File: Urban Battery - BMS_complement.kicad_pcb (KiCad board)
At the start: 2 copper layers, 154 x 84.1 mm, 57 parts, among them J1 BMS IO, J10 E-Stop, J11 Contactor Connector, J12 Thermistor, J13 Thermistor, J14 Thermistor, J15 short pins, J16 short pins, J17 short pins, J18 short pins, J19 Test-pins, J2 OLED Header, J20 Test-pins, J21 Test-pins, J22 Test-pins, J23 Test-pins, J24 Test-pins, J25 Test-pins, J26 Test-pins, J27 Test-pins, J3 CAN, J4 CAN, J5 Charge Connector, J6 Battery Connector, J7 E-Stop, J8 E-Stop, J9 E-Stop, K1 Charge_Relay, K2 Contactor_Relay, SW1 SW_SPST, SW2 SW_DPDT_x2, SW3 CAN_TERM, U1 MCP2515-I/SO, U2 MCP2561/2, U3 LM2576HVS-12, Y1 8MHz

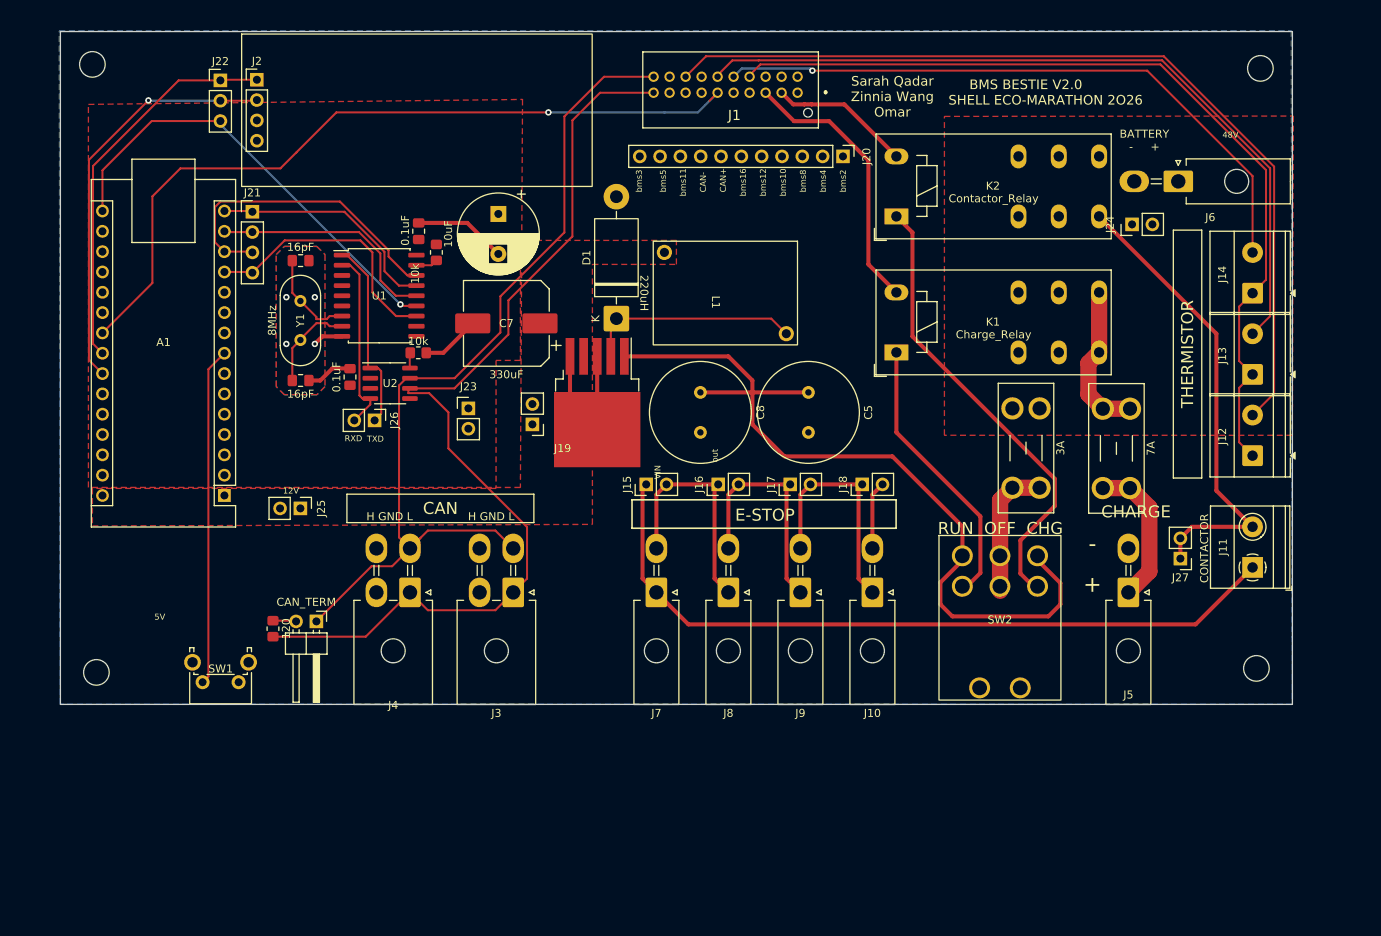
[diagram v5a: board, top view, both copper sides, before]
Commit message: routed BMS test pins, edited some labels
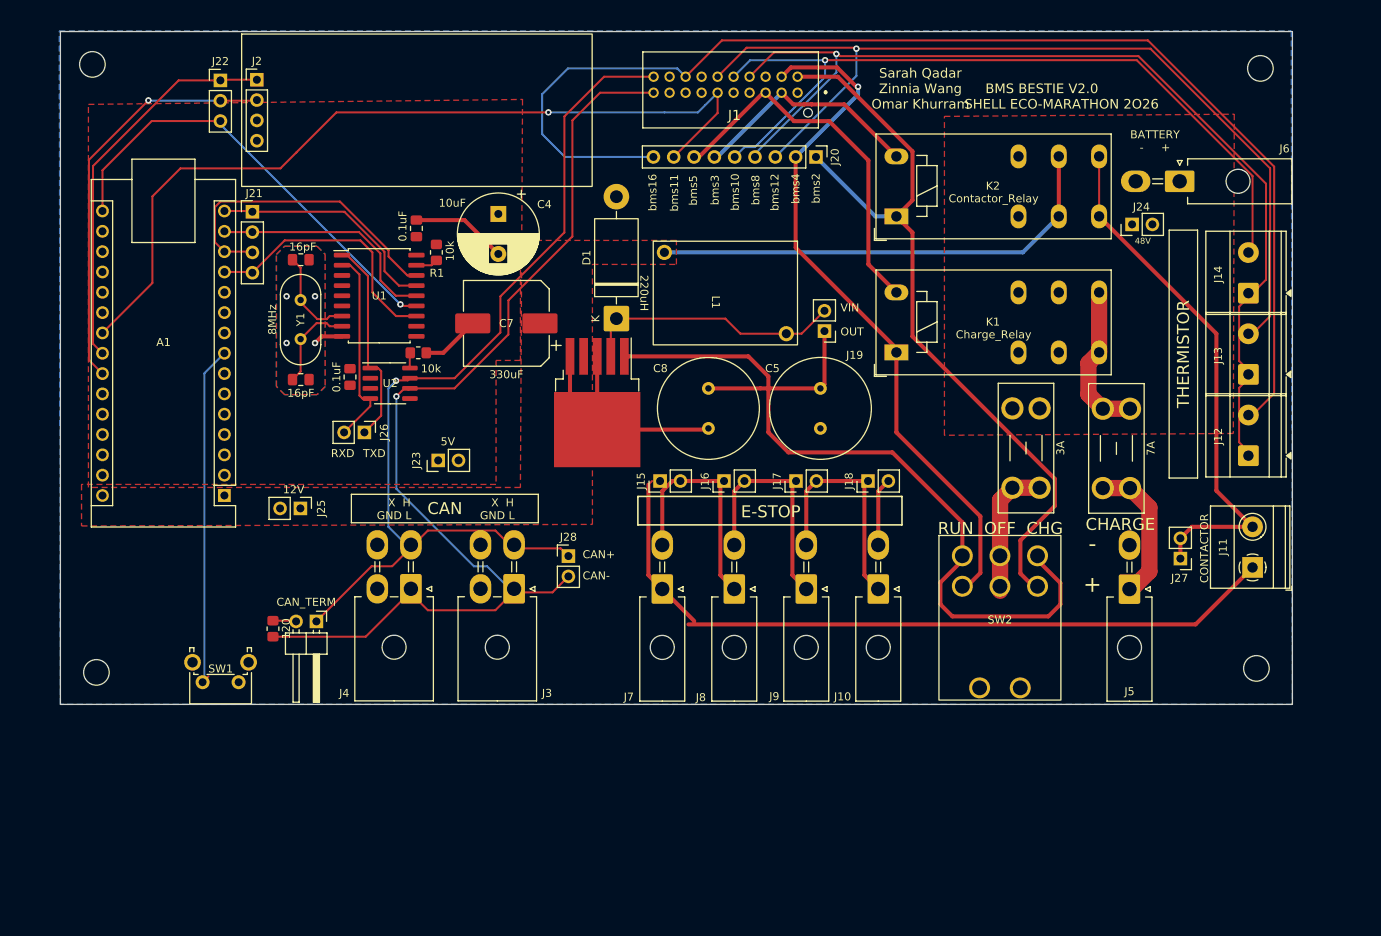
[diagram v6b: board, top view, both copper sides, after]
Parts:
- added J28: Test-pins, Connector_PinHeader_2.54mm:PinHeader_1x02_P2.54mm_Vertical, F.Cu at (138.0, 118.0)
- J20: footprint Connector_PinHeader_2.54mm:PinHeader_1x11_P2.54mm_Vertical -> Connector_PinHeader_2.54mm:PinHeader_1x09_P2.54mm_Vertical
- moved J19 38.3 mm to (170.0, 89.8)
- moved J23 7.52 mm to (121.7, 106.0), turned to 90 degrees
- moved J20 3.37 mm to (168.9, 68.1)
- moved J26 1.97 mm to (112.5, 102.5)
- moved J15 1.79 mm to (149.5, 108.6)
- moved C5 1.58 mm to (169.5, 97.0)
- moved C8 1.12 mm to (155.5, 97.0)
- moved G*** 1.11 mm to (90.0, 120.5)
- moved J10 0.85 mm to (176.7, 122.1)
- moved J16 0.85 mm to (157.5, 108.6)
- moved J17 0.85 mm to (166.5, 108.6)
- moved J18 0.85 mm to (175.5, 108.6)
- moved J7 0.85 mm to (149.7, 122.1)
- moved J8 0.85 mm to (158.7, 122.1)
- moved J9 0.85 mm to (167.7, 122.1)
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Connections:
- J20 pad 3: bms8 -> bms12
- J20 pad 4: bms10 -> bms8
- J20 pad 5: bms12 -> bms10
- J20 pad 6: bms16 -> bms3
- J20 pad 7: CAN+ -> bms5
- J20 pad 8: CAN- -> bms11
- J20 pad 9: bms11 -> bms16
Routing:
- net +12V: track 0.00 -> 58.7 mm
- net bms4: track 35.1 -> 87.9 mm, vias 0 -> 1
- net bms16: track 112.5 -> 153.9 mm
- net bms2: track 57.7 -> 98.0 mm
- net bms12: track 97.2 -> 116.1 mm, vias 0 -> 1
- net bms10: track 81.3 -> 99.0 mm
- net bms8: track 110.0 -> 127.4 mm, vias 0 -> 1
- net bms5: track 34.3 -> 46.6 mm
- net bms3: track 17.7 -> 29.4 mm
- net CAN+: track 112.0 -> 121.4 mm, vias 0 -> 1
- net Buck_VIN: track 101.6 -> 110.6 mm
- net bms11: track 97.1 -> 106.0 mm
- net GND: track 56.7 -> 65.3 mm
- net CAN-: track 124.9 -> 132.5 mm, vias 0 -> 1
- net Net-(J11-Pin_2): track 59.6 -> 67.1 mm
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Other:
- board text added: "OUT"
- board text added: "Sarah Qadar Zinnia Wang Omar Khurram"
- board text added: "X H GND L"
- board text removed: "H GND L"
- board text removed: "Sarah Qadar Zinnia Wang Omar"
- board text removed: "out"

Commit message: resolving minor overlap and clearance issues
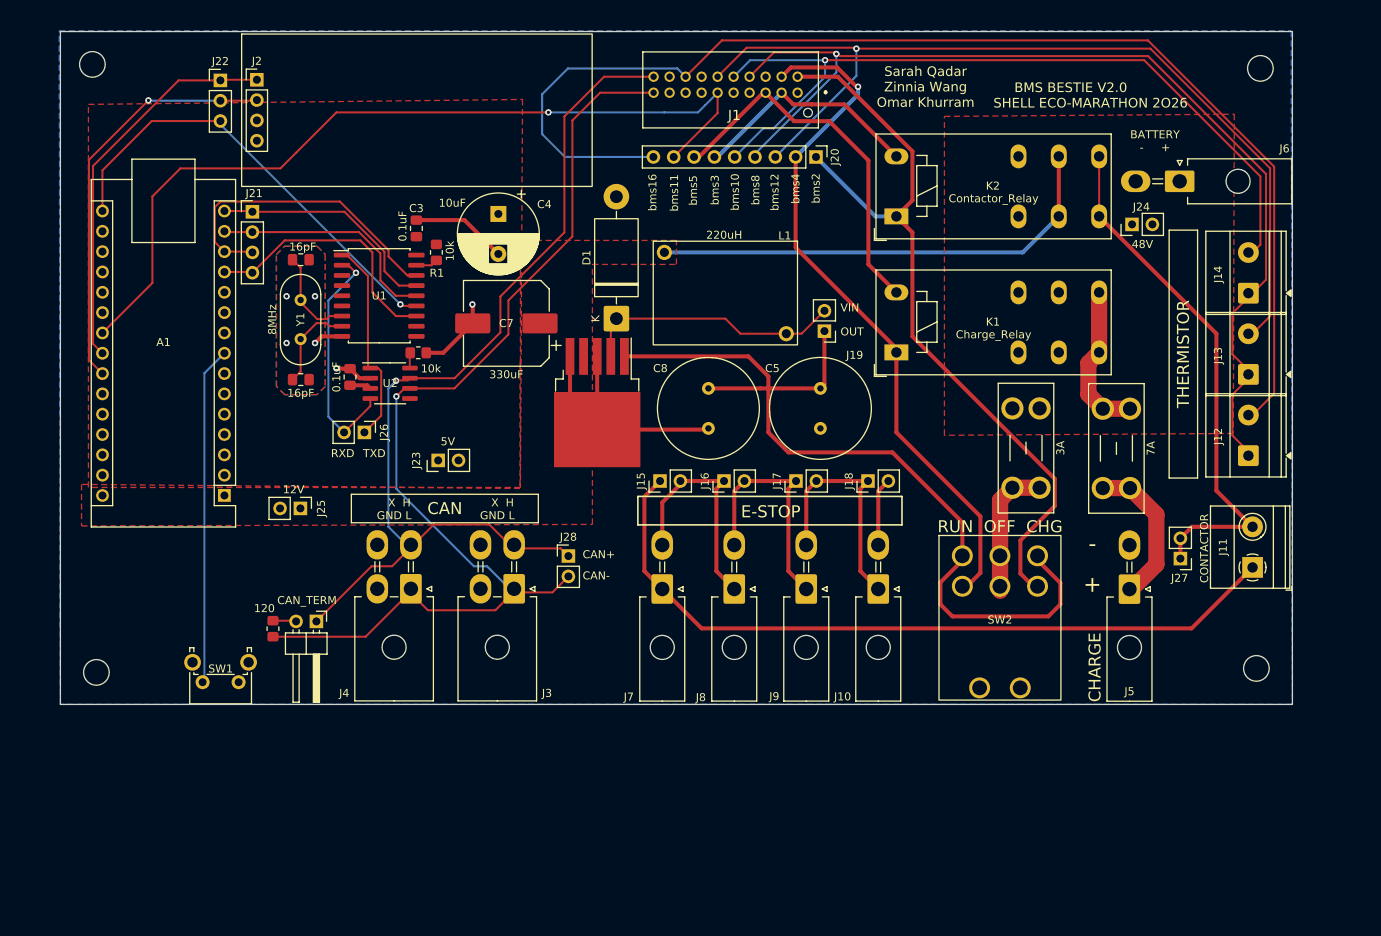
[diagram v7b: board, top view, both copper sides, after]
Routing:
- net GND: track 65.3 -> 72.4 mm, vias 4 -> 6
- net Net-(J26-Pin_2): track 24.9 -> 29.9 mm, vias 0 -> 1
- net +5V: track 0.00 -> 2.70 mm
- net bms8: track 127.4 -> 129.5 mm
- net bms10: track 99.0 -> 100.3 mm
- net Net-(A1-D5): track 43.3 -> 42.2 mm
- net Net-(J15-Pin_2): track 29.4 -> 28.6 mm
- net Charge: track 18.5 -> 19.3 mm
- net Net-(J11-Pin_1): track 93.5 -> 94.2 mm
- net CAN+: track 121.4 -> 122.1 mm

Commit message: Cleaned up labelling, overlap and logo; GND plane connections remain sus
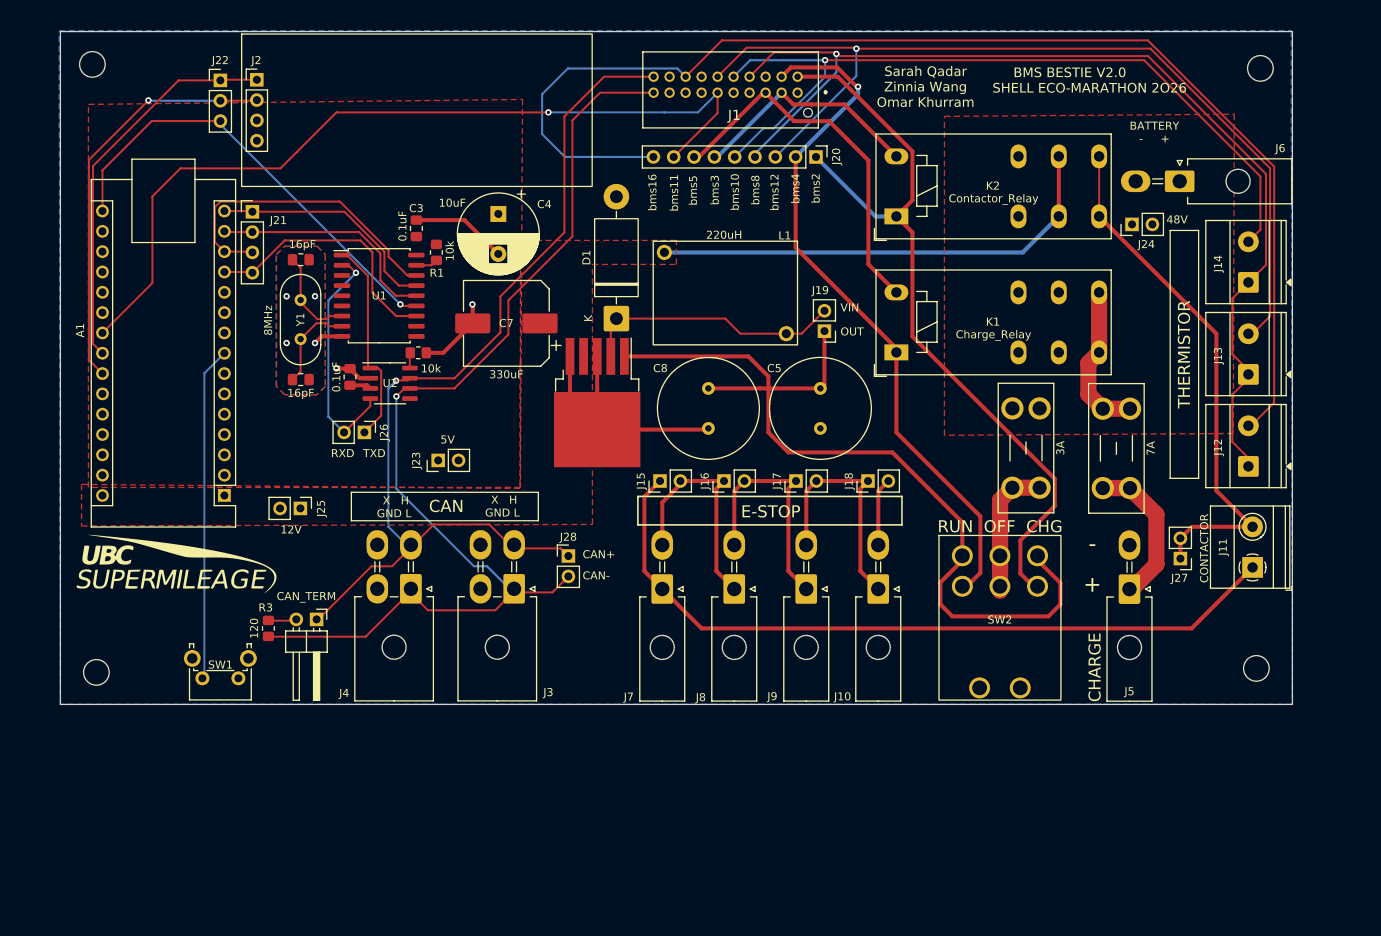
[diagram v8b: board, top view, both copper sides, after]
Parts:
- removed the G*** at (90.0, 120.5)
- added G***: LOGO, BMS_Custom_Footprints:sm_logo_2026, F.Cu at (89.0, 119.0)
- moved J14 1.34 mm to (223.0, 83.8)
- moved J12 1.34 mm to (223.0, 106.8)
- moved R3 0.57 mm to (100.5, 127.0)
- moved SW1 0.49 mm to (96.8, 133.2)
- moved SW3 0.25 mm to (106.5, 125.9)
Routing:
- net bms10: track 100.3 -> 98.5 mm
- net bms16: track 153.9 -> 155.3 mm
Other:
- board text added: "R3"
